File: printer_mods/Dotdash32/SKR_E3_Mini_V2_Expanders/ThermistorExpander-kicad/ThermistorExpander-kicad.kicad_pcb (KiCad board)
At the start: 2 copper layers, 26 x 19.7 mm, 8 parts, among them J1 Conn_02x03_Odd_Even, J2 Conn_01x02, J3 Conn_01x02, J4 Conn_01x02

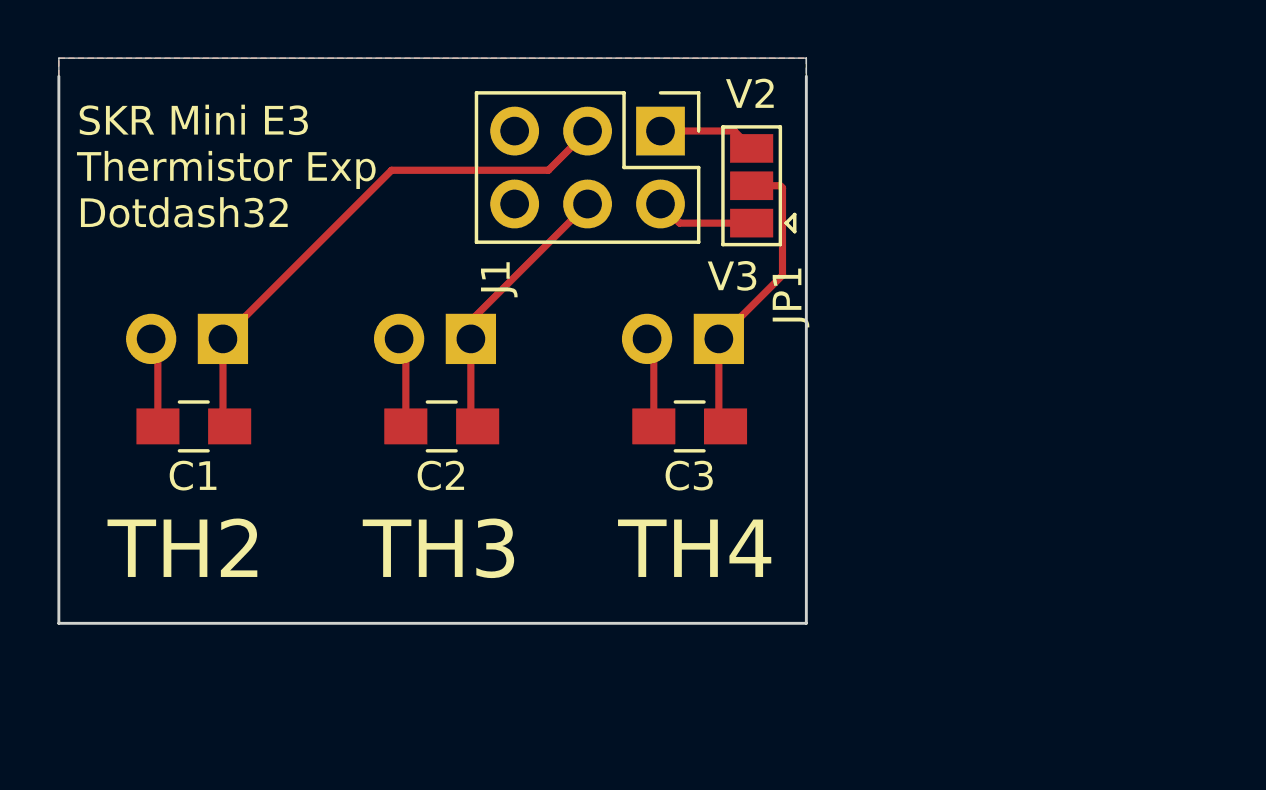
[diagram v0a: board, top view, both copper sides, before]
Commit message: feat: move JST headers to avoid EXP1 port
but now interfering with the USB port, which is more useful.
So maybe we try to use the vertical headers and admit defeat?
sad bears, sad beers
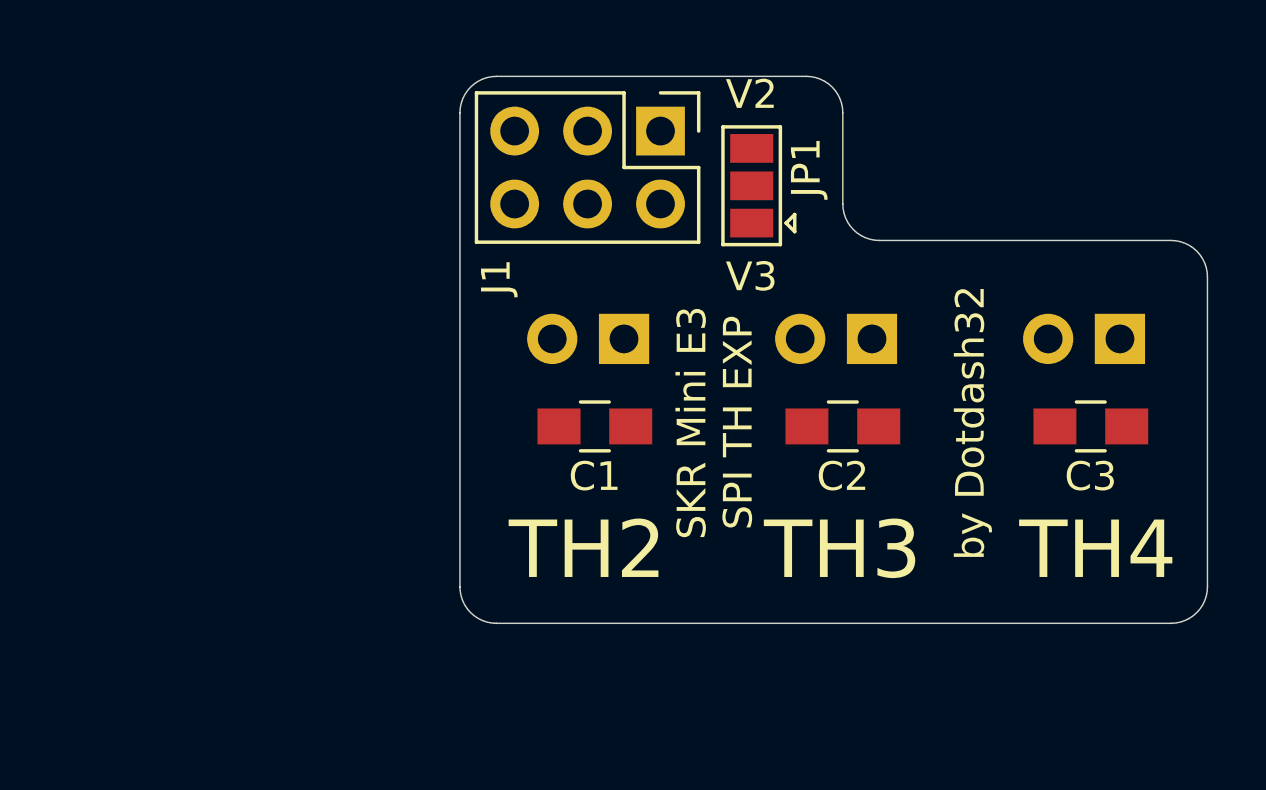
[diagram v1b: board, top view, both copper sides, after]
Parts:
- moved C2 14.0 mm to (132.1, 85.2)
- moved C3 14.0 mm to (140.7, 85.2)
- moved C1 14.0 mm to (123.4, 85.2)
- moved J2 14.0 mm to (124.5, 82.2)
- moved J3 14.0 mm to (133.1, 82.2)
- moved J4 14.0 mm to (141.7, 82.2)
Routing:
- net /TH2: track 18.8 -> 0.00 mm
- net /TH4: track 10.4 -> 0.00 mm
- net /TH3: track 9.53 -> 0.00 mm
- net GND: track 9.43 -> 0.00 mm
- net /V3.0: track 3.45 -> 0.00 mm
- net /V2.0: track 3.43 -> 0.00 mm
- removed copper zone on B.Cu, net GND
- removed copper zone on F.Cu, net GND
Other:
- board size 26 x 19.7 mm -> 26 x 19.1 mm
- board text added: "SKR Mini E3 SPI TH EXP"
- board text added: "VORON Design"
- board text added: "by Dotdash32"
- board text removed: "SKR Mini E3 Thermistor Exp Dotdash32"

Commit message: feat: use straight JSTs, clear existing SKR ports
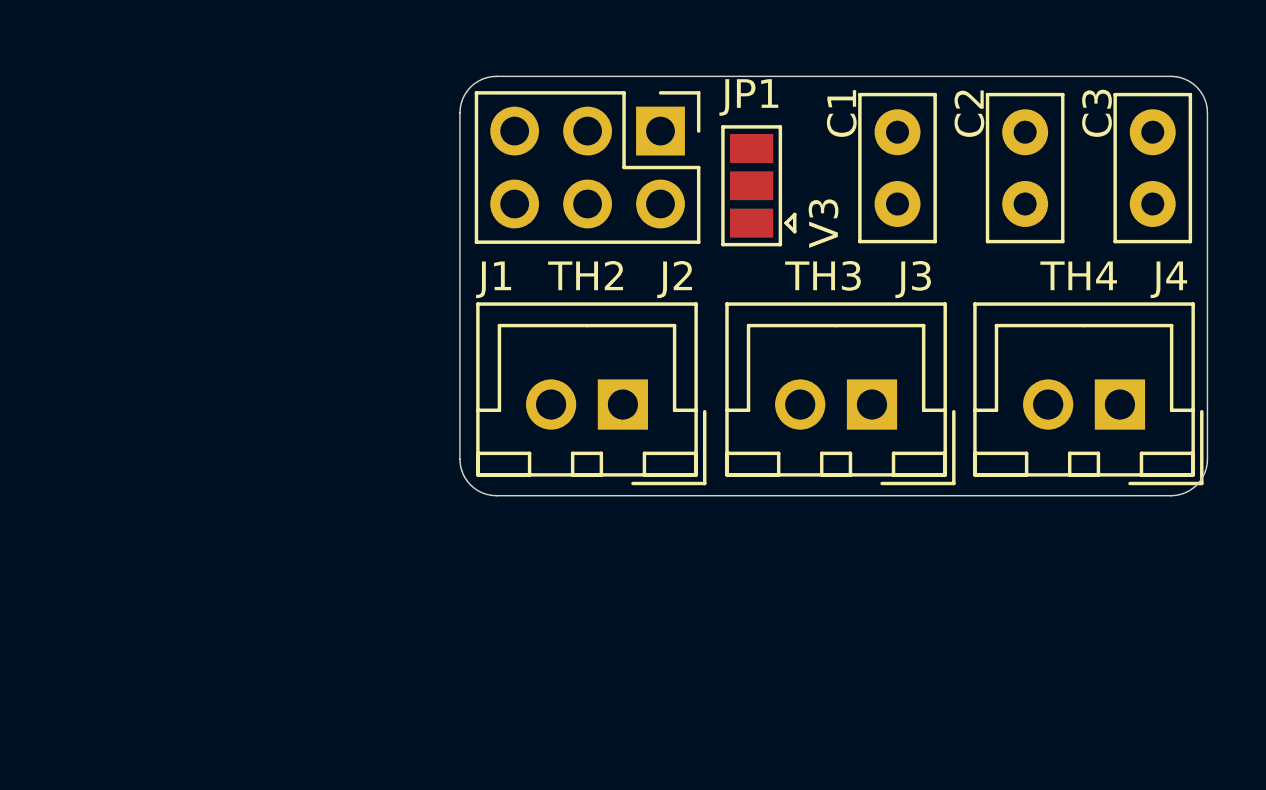
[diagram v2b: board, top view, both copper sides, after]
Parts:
- C1, C2, C3: footprint Capacitors_SMD:C_0805_HandSoldering -> Capacitors_THT:C_Disc_D5.0mm_W2.5mm_P2.50mm
- J2, J3, J4: footprint Connectors_JST:JST_XH_S02B-XH-A_02x2.50mm_Angled -> Connectors_JST:JST_XH_B02B-XH-A_02x2.50mm_Straight; moved to F.Cu
- moved C1 13.1 mm to (134.0, 77.5), turned to 90 degrees
- moved C2 10.0 mm to (138.4, 77.5), turned to 90 degrees
- moved C3 8.04 mm to (142.9, 77.5), turned to 90 degrees
- moved J2 2.29 mm to (124.4, 84.5)
- moved J3 2.29 mm to (133.1, 84.5)
- moved J4 2.29 mm to (141.7, 84.5)
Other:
- board size 26 x 19.1 mm -> 26 x 14.6 mm
- board text added: "SKR Mini E3 SPI Thermistor Expander by Dotdash32 (JDeW)"
- board text removed: "SKR Mini E3 SPI TH EXP"
- board text removed: "V2"
- board text removed: "VORON Design"
- board text removed: "by Dotdash32"

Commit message: fix: actually route the traces please
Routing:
- net /TH2: track 0.00 -> 23.8 mm
- net /TH4: track 0.00 -> 23.6 mm
- net /TH3: track 0.00 -> 22.0 mm
- net /V3.0: track 0.00 -> 3.45 mm
- net /V2.0: track 0.00 -> 3.43 mm
- added copper zone on B.Cu, net GND
- added copper zone on F.Cu, net GND

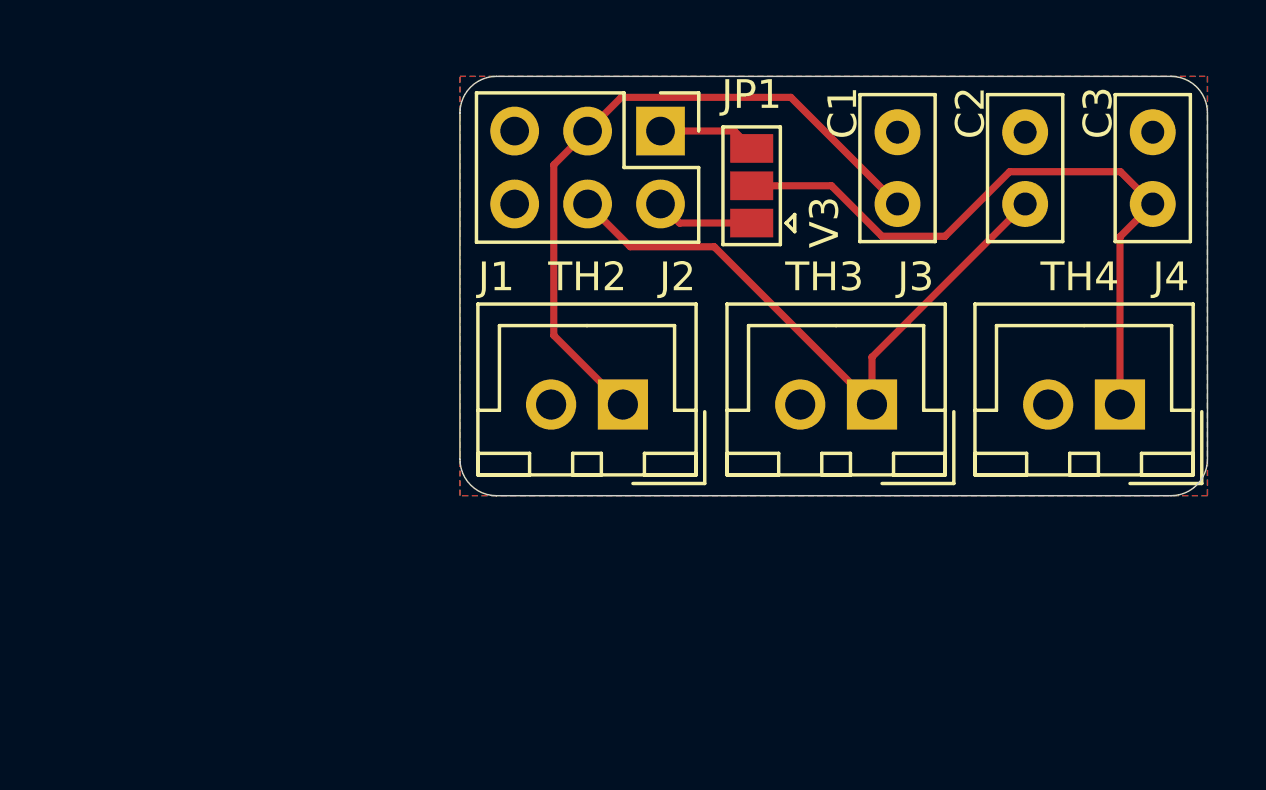
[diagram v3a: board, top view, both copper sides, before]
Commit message: feat: shrink TH_exp to be more space efficient
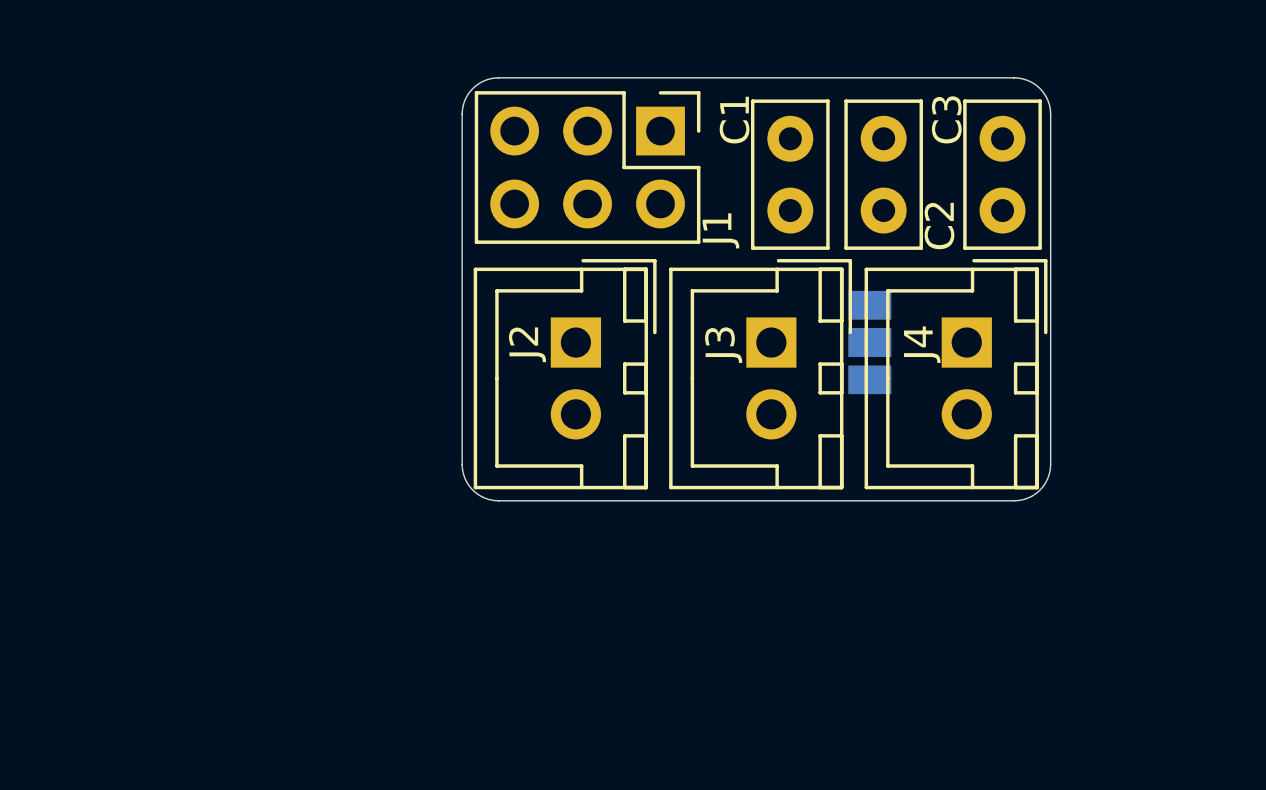
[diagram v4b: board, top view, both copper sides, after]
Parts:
- JP1: moved to B.Cu
- moved JP1 6.84 mm to (133.0, 82.3), turned to 270 degrees
- moved J4 5.75 mm to (136.4, 82.3), turned to 270 degrees
- moved C3 5.24 mm to (137.6, 77.7)
- moved C2 4.93 mm to (133.5, 77.7)
- moved J3 4.12 mm to (129.6, 82.3), turned to 270 degrees
- moved C1 3.74 mm to (130.3, 77.7)
- moved J2 2.71 mm to (122.8, 82.3), turned to 270 degrees
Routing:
- net /TH2: track 23.8 -> 0.00 mm
- net /TH4: track 23.6 -> 0.00 mm
- net /TH3: track 22.0 -> 0.00 mm
- net /V3.0: track 3.45 -> 0.00 mm
- net /V2.0: track 3.43 -> 0.00 mm
- removed copper zone on B.Cu, net GND
- removed copper zone on F.Cu, net GND
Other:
- board size 26 x 14.6 mm -> 20.5 x 14.7 mm
- board text added: "SPI TH Exp by Dotdash32 (JDeW)"
- board text added: "V2"
- board text removed: "SKR Mini E3 SPI Thermistor Expander by Dotdash32 (JDeW)"

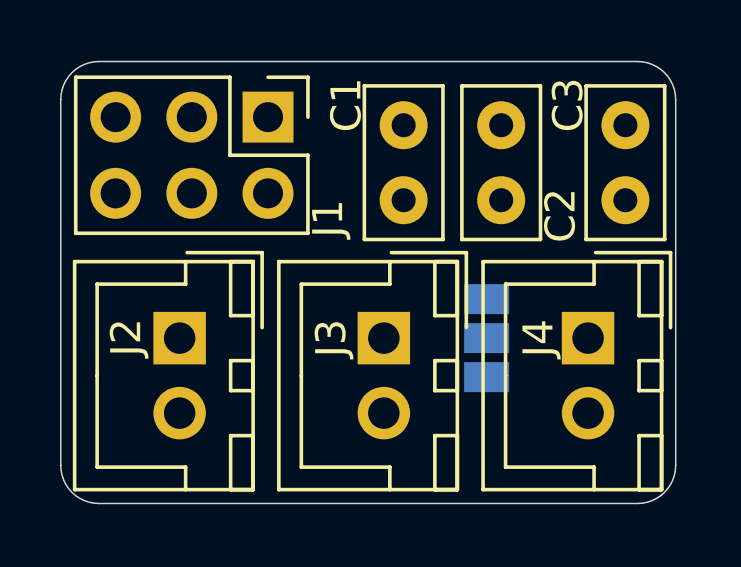
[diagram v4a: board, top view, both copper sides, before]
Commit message: chore: routing TH exp in new formfactor
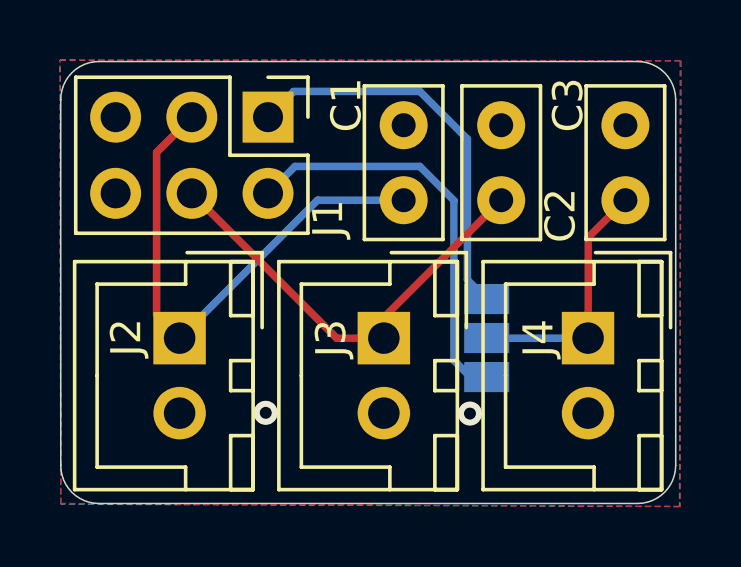
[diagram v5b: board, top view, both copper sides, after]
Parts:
- turned JP1 to 90 degrees
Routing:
- net /TH2: track 0.00 -> 17.5 mm
- net /TH3: track 0.00 -> 14.6 mm
- net /V3.0: track 0.00 -> 13.7 mm
- net /V2.0: track 0.00 -> 13.3 mm
- net /TH4: track 0.00 -> 8.49 mm
- net GND: vias 0 -> 2
- added copper zone on B.Cu, net GND
- added copper zone on F.Cu, net GND
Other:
- board text added: "JLCJLCJLCJLC"

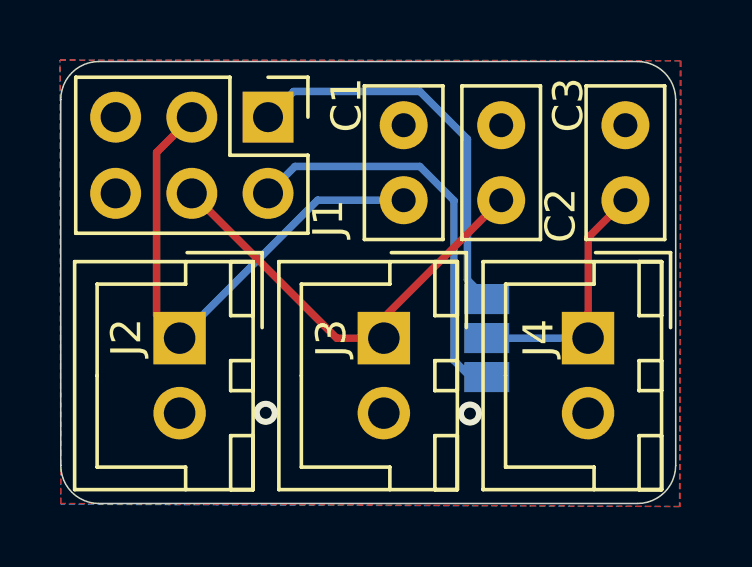
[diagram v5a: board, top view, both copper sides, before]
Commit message: feat: cleaning and preping TH expander
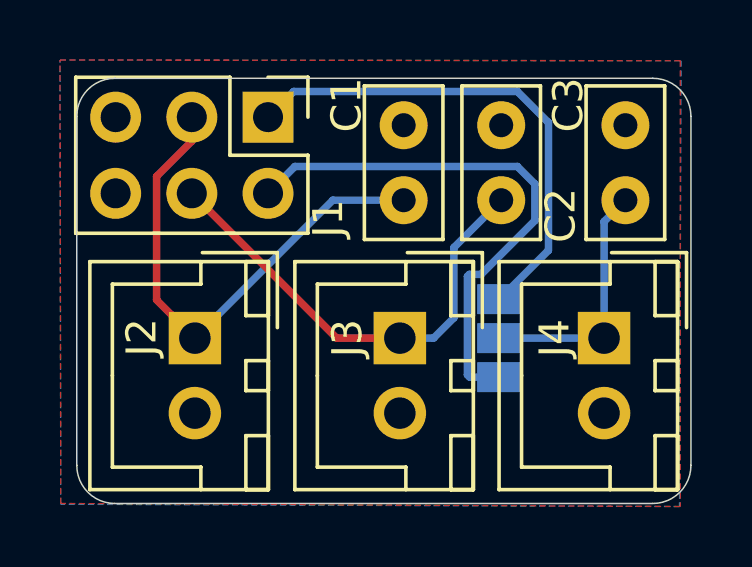
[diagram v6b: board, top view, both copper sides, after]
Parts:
- moved J3 0.53 mm to (130.1, 82.3)
- moved J4 0.53 mm to (136.9, 82.3)
- moved J2 0.51 mm to (123.3, 82.3)
- moved JP1 0.43 mm to (133.5, 82.3)
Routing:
- net /V3.0: track 13.7 -> 18.1 mm
- net /V2.0: track 13.3 -> 16.7 mm
- net /TH3: track 14.6 -> 15.6 mm
- net GND: vias 2 -> 0
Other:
- board size 20.5 x 14.7 mm -> 20.5 x 14.2 mm

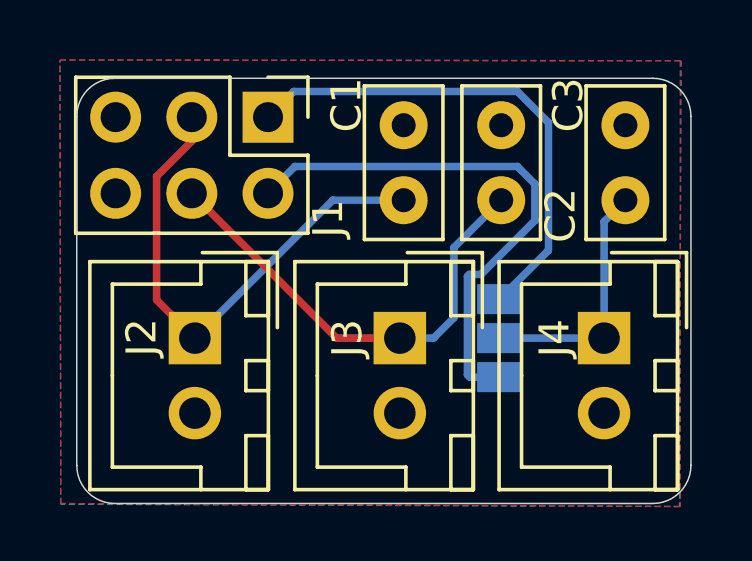
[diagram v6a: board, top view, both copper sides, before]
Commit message: feat|docs: 2x4 SPI header, readme updates
also re-routing some silly decisions, cleaning schematic
Also moving some readme-stuff around for
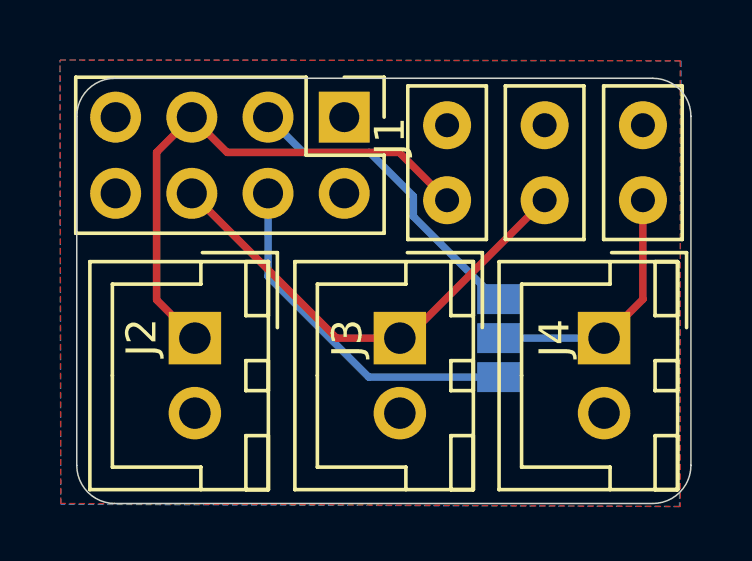
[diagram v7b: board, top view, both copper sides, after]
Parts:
- J1: value Conn_02x03_Odd_Even -> SPI1_breakaway; footprint Pin_Headers:Pin_Header_Straight_2x03_Pitch2.54mm -> Pin_Headers:Pin_Header_Straight_2x04_Pitch2.54mm
- moved J1 2.54 mm to (128.3, 74.9)
- moved C1 1.45 mm to (131.7, 77.7)
- moved C2 1.45 mm to (135.0, 77.7)
- moved C3 0.58 mm to (138.2, 77.7)
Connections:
- J1 pad 1: /V2.0 -> Net-(J1-Pad1)
- J1 pad 2: /V3.0 -> GND
- J1 pad 3: /TH2 -> /V2.0
- J1 pad 4: /TH3 -> /V3.0
- J1 pad 5: Net-(J1-Pad5) -> /TH2
- J1 pad 6: GND -> /TH3
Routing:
- net /V3.0: track 18.1 -> 11.9 mm
- net /V2.0: track 16.7 -> 10.6 mm
- net /TH2: track 17.2 -> 18.0 mm
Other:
- board text added: "Dotdash32 (JDeW)"
- board text added: "JLCJLCJLC"
- board text added: "SPI TH Exp V1.0"
- board text removed: "JLCJLCJLCJLC"
- board text removed: "SPI TH Exp by Dotdash32 (JDeW)"
